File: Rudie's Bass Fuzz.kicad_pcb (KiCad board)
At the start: 2 copper layers, 25 x 50 mm, 19 parts, among them J1 Conn_01x01_Male, J2 Conn_01x01_Male, J3 Conn_01x01_Male, J4 Conn_01x01_Male, J5 Conn_01x01_Male, J6 Conn_01x01_Male, Q1 BC549

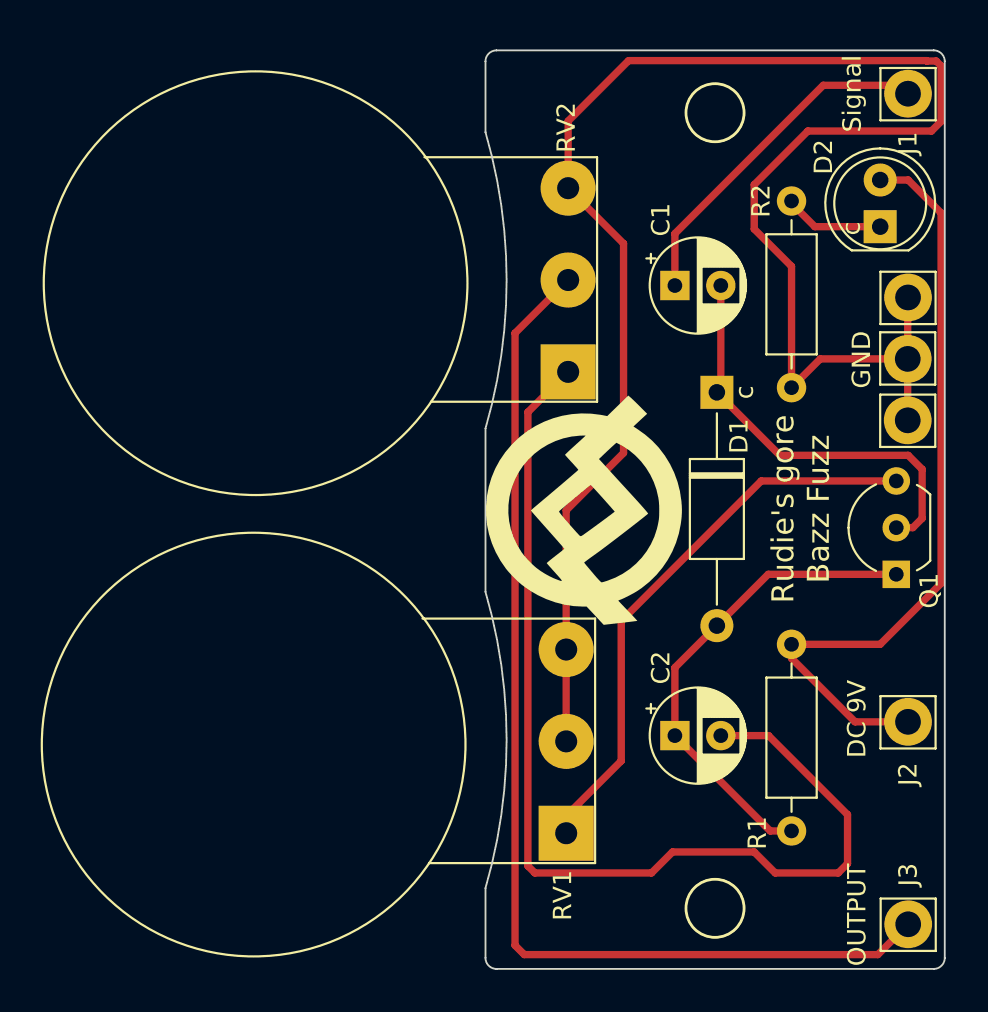
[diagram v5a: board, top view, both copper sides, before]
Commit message: moved connectors inwards a bit and added rounded design
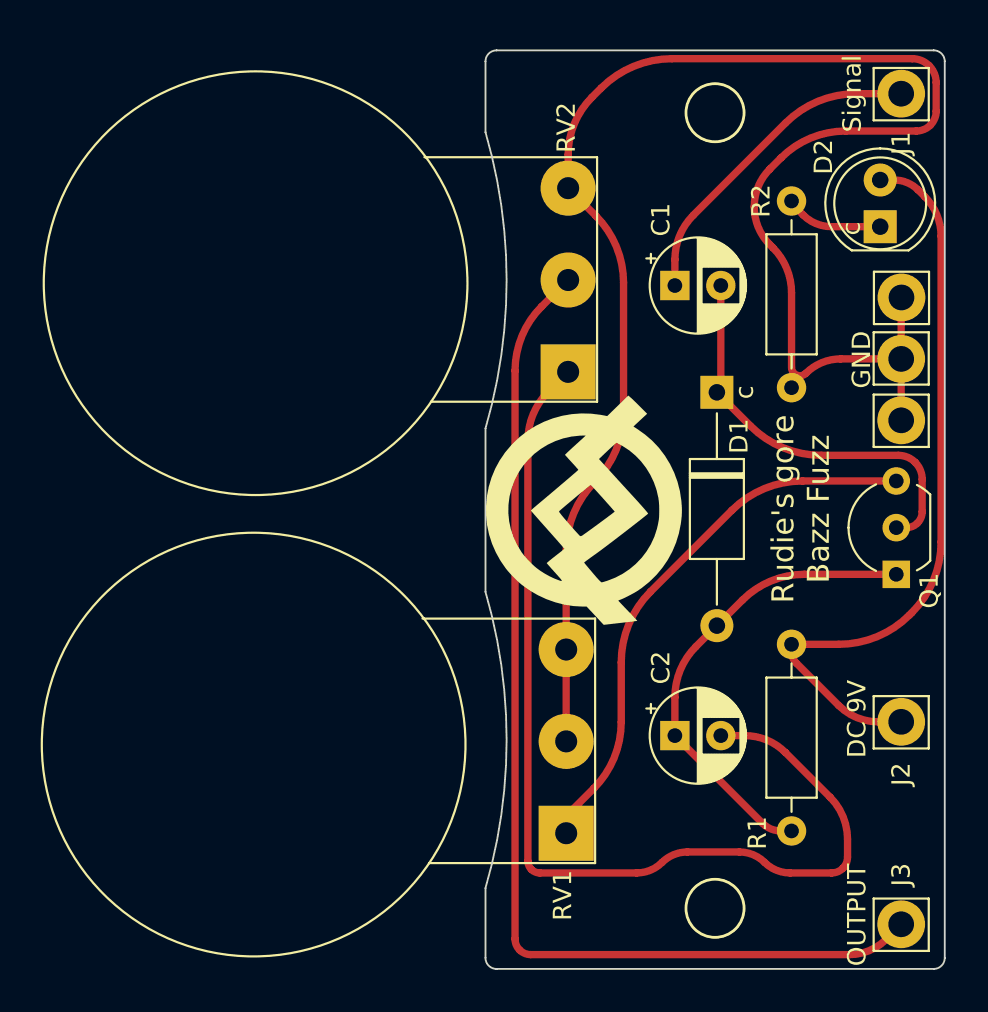
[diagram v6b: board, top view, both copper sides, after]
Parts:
- moved J3 0.38 mm to (181.2, 90.2)
- moved J1 0.37 mm to (181.2, 45.0)
- moved J2 0.37 mm to (181.2, 79.2)
- moved J4 0.36 mm to (181.2, 56.0)
- moved J5 0.36 mm to (181.2, 62.7)
- moved J6 0.36 mm to (181.2, 59.4)
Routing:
- net GND: track 98.3 -> 93.0 mm
- net 9V: track 42.3 -> 40.8 mm
- net Signal: track 19.0 -> 17.9 mm
- net Net-(C2-Pad2): track 57.9 -> 56.9 mm
- net Output: track 59.7 -> 58.9 mm
- net Net-(Q1-Pad3): track 30.9 -> 30.1 mm
- net Net-(C1-Pad2): track 23.1 -> 22.5 mm

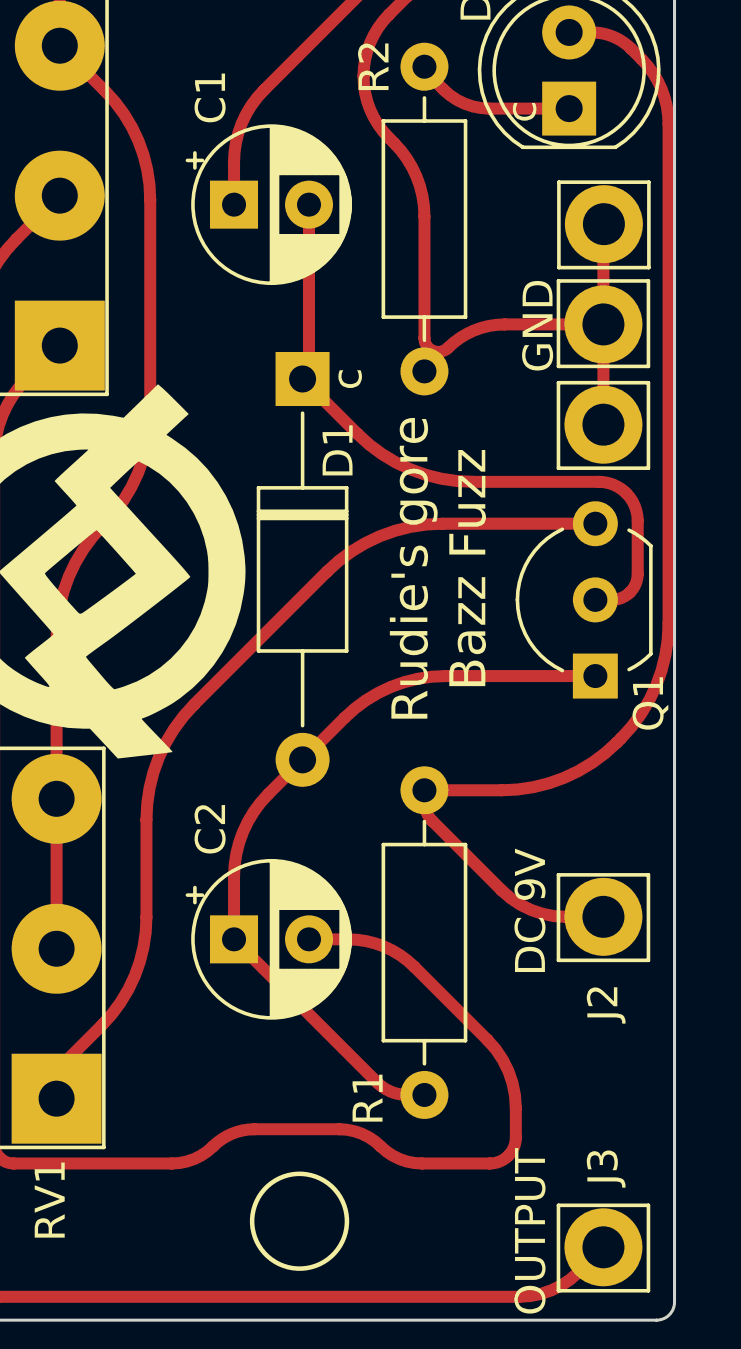
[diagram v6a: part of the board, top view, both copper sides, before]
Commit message: Finalized design
Improved silkscreen and tracks a bit.
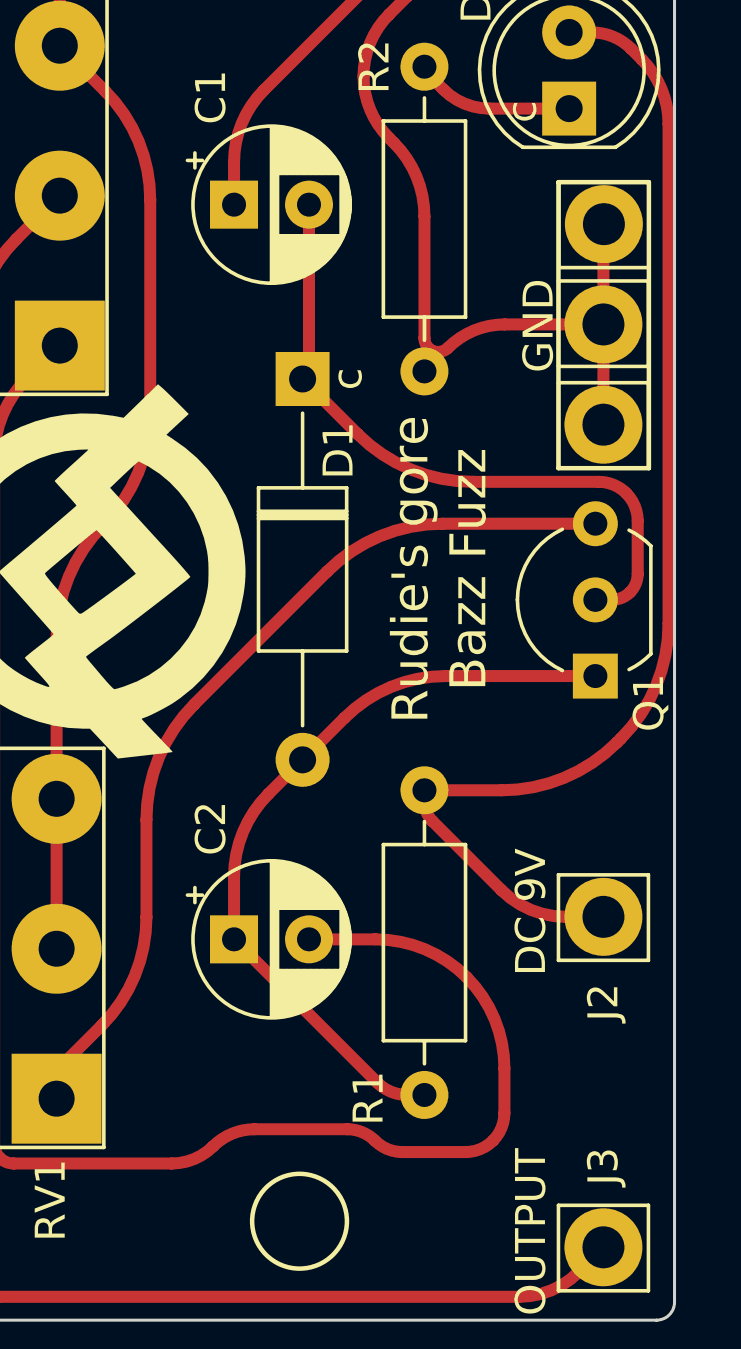
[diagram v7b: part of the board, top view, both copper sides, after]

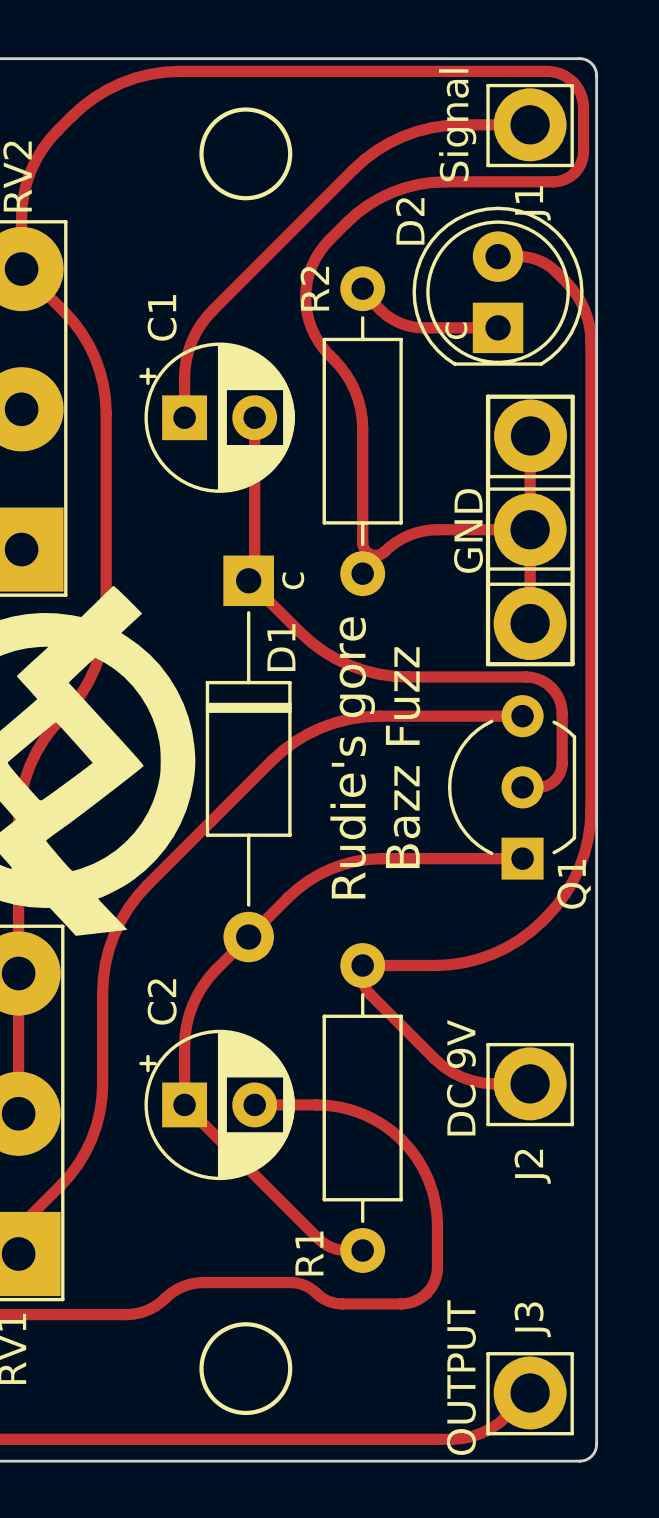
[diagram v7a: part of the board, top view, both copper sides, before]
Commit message: silkscreen cleanup
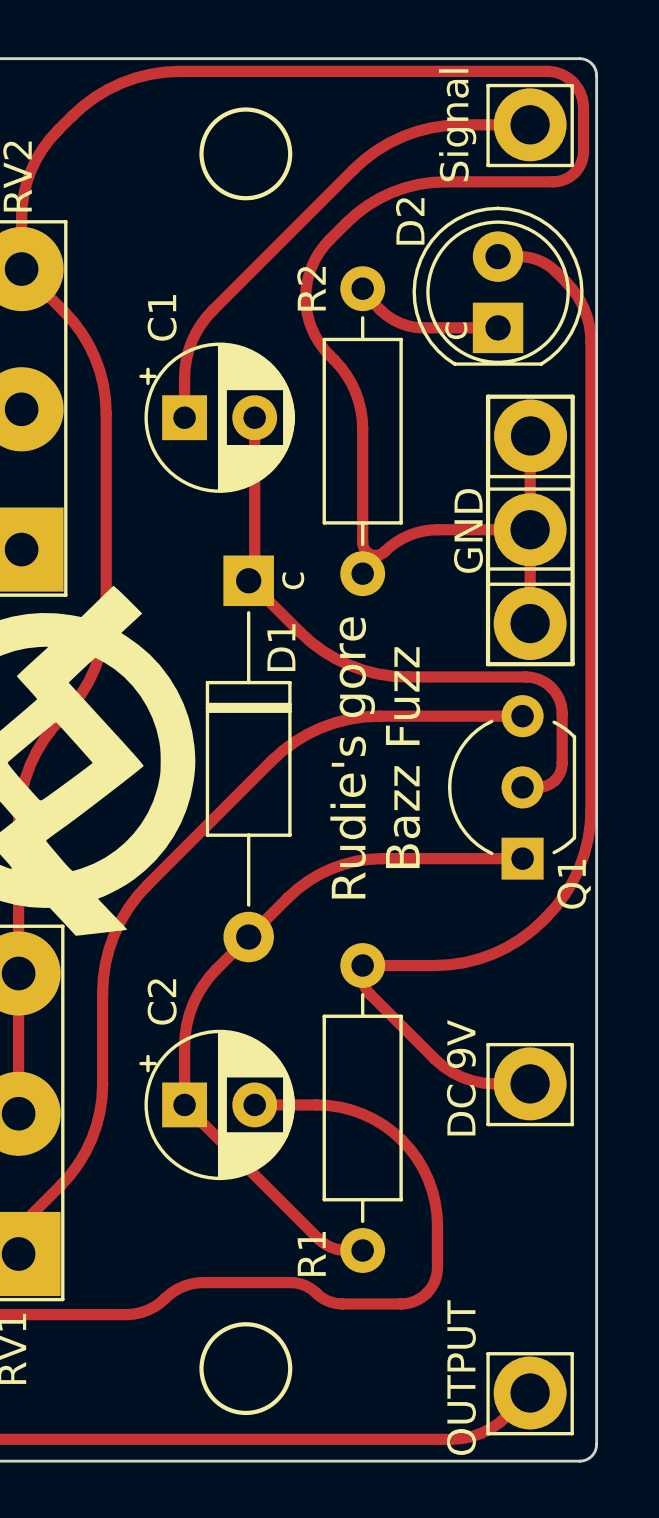
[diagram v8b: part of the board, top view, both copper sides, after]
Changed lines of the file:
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@@
     (property "Sheetname" "")
     (attr through_hole)
-    (fp_text reference "J1" (at 0 2.7 90) (layer "F.SilkS")
+    (fp_text reference "J1" (at 0 2.7 90) (layer "F.SilkS") hide
       (effects (font (size 1 1) (thickness 0.15)))
     )
@@
     (property "Sheetname" "")
     (attr through_hole)
-    (fp_text reference "R2" (at 0 1.66 90) (layer "F.SilkS")
+    (fp_text reference "R2" (at 0 1.778 90) (layer "F.SilkS")
       (effects (font (size 1 1) (thickness 0.15)))
     )
@@
     (property "Sheetname" "")
     (attr through_hole)
-    (fp_text reference "R1" (at 10.27 1.86 90) (layer "F.SilkS")
+    (fp_text reference "R1" (at 10.287 1.778 90) (layer "F.SilkS")
       (effects (font (size 1 1) (thickness 0.15)))
     )
@@
     (property "Sheetname" "")
     (attr through_hole)
-    (fp_text reference "J2" (at 0 2.85 270) (layer "F.SilkS")
+    (fp_text reference "J2" (at 0 2.85 270) (layer "F.SilkS") hide
       (effects (font (size 1 1) (thickness 0.15)))
     )
@@
     (property "Sheetname" "")
     (attr through_hole)
-    (fp_text reference "J3" (at 0 -2.7 90) (layer "F.SilkS")
+    (fp_text reference "J3" (at 0 -2.7 90) (layer "F.SilkS") hide
       (effects (font (size 1 1) (thickness 0.15)))
     )
@@
   (gr_arc (start 183.6 92) (mid 183.424264 92.424264) (end 183 92.6) (layer "Edge.Cuts") (width 0.1))
   (gr_arc (start 183 42.6) (mid 183.424264 42.775736) (end 183.6 43.2) (layer "Edge.Cuts") (width 0.1))
-  (gr_text "Rudie's gore \nBazz Fuzz V0.1\n15-12-2022" (at 178.181 77.47 90) (layer "B.SilkS")
+  (gr_text "Rudie's gore \nBazz Fuzz V0.1\n15-12-2022" (at 177.927 76.835 90) (layer "B.SilkS")
     (effects (font (size 1 1) (thickness 0.15)) (justify left mirror))
   )
